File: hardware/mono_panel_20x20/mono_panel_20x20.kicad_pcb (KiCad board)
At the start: 2 copper layers, 136.3 x 136.3 mm, 402 parts

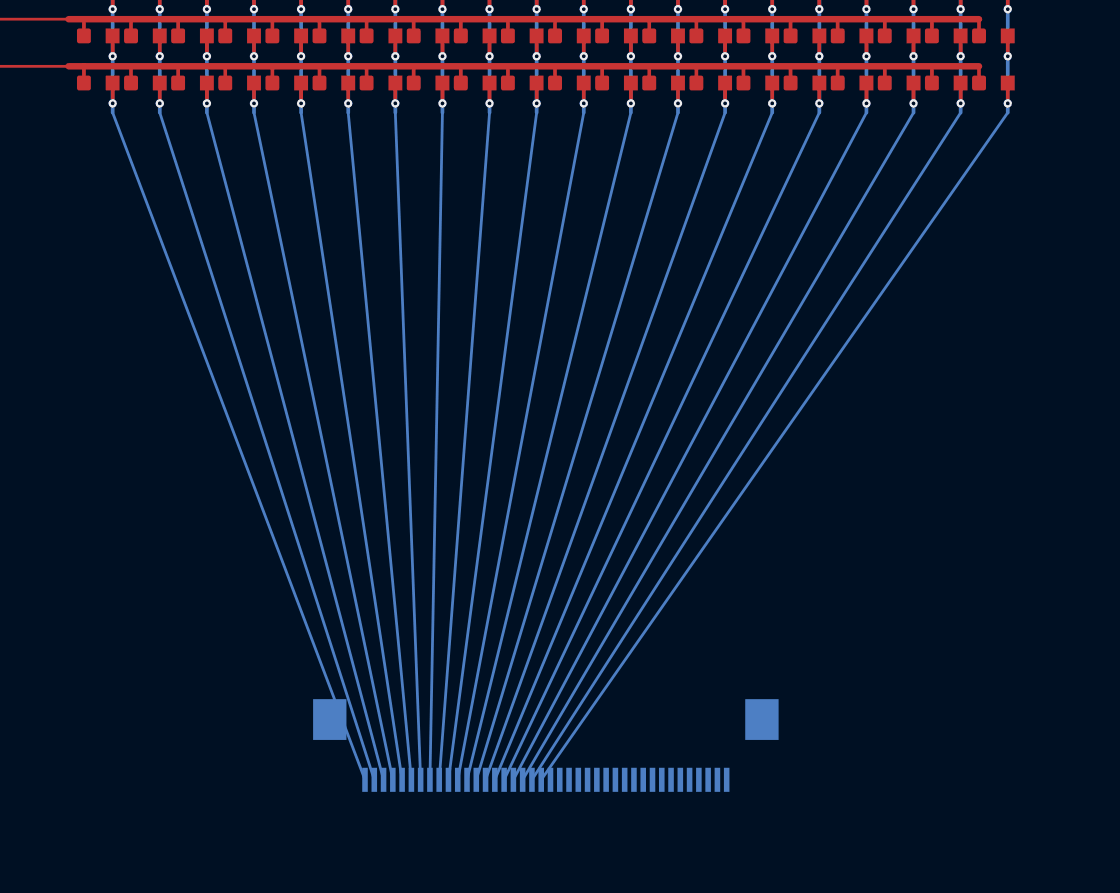
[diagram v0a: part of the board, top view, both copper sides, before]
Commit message: Fix mono panel fan-in DRC and spacious electronics placement.
Route rows through a U-turn via row and drop columns onto FFC pad centerlines so both LED panels are geometrically DRC-clean. Widen the electronics board, clear courtyards and silk, and record the fan-in constraints in cursor.md.

Co-authored-by: illiapliukhin <illiapliukhin@users.noreply.github.com>
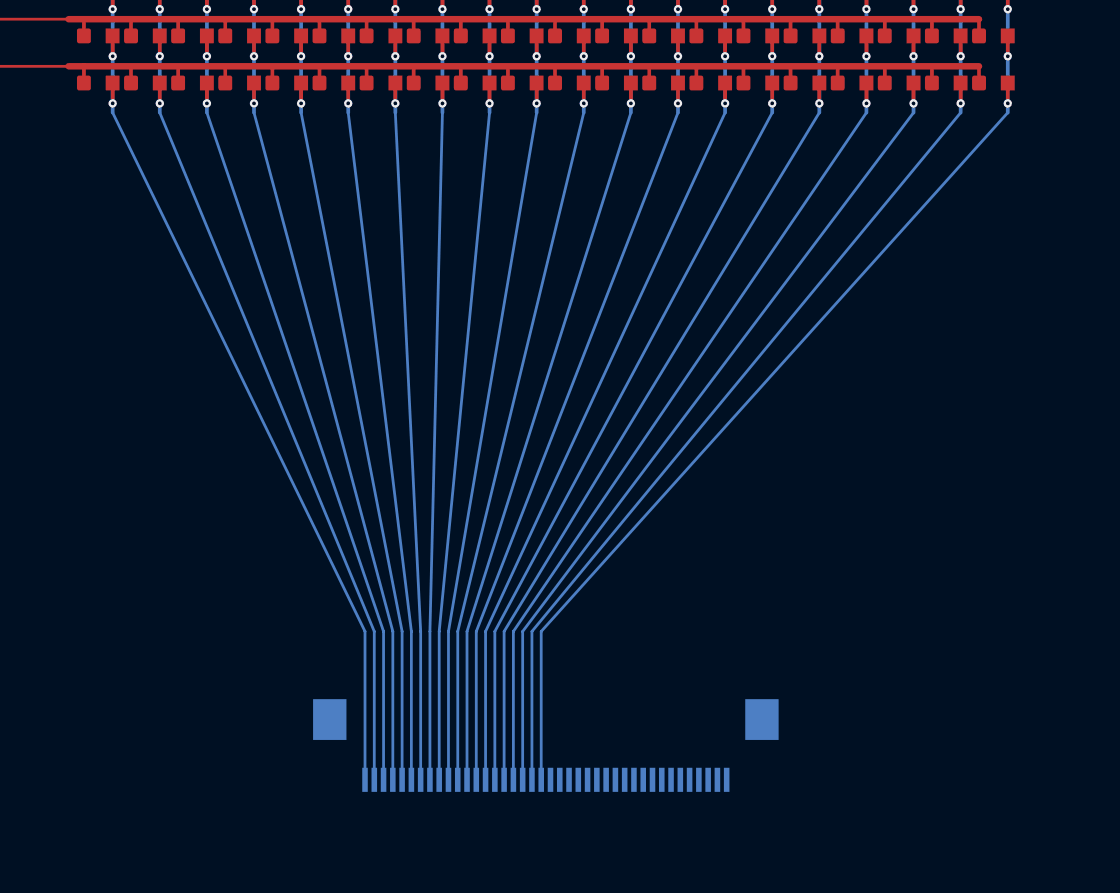
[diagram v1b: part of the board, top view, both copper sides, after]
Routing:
- net COL_20: track 114.7 -> 116.4 mm
- net COL_19: track 113.5 -> 115.0 mm
- net COL_18: track 112.4 -> 113.8 mm
- net COL_17: track 111.5 -> 112.6 mm
- net COL_16: track 110.5 -> 111.5 mm
- net COL_15: track 109.7 -> 110.5 mm
- net COL_01: track 109.2 -> 109.9 mm
- net COL_14: track 109.0 -> 109.6 mm
